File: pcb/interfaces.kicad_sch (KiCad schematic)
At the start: 21 parts, among them J10 BM08B-SRSS-TB, J14 BM03B-SRSS-TB, J3 BM03B-SRSS-TB, J8 BM04B-SRSS-TB, J9 BM04B-SRSS-TB, Q1 MMBT2222A

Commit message: Renamed peripherals to interfaces; added test points; added led jumper
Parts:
- TP29, TP30, TP31, TP32, TP33, TP34, TP35, TP36: value TP -> ~
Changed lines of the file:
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@@
 			)
 		)
-		(property "Value" "TP"
+		(property "Value" "~"
 			(at 113.03 74.168 0)
 			(effects
@@
 			)
 		)
-		(property "Value" "TP"
+		(property "Value" "~"
 			(at 123.19 74.168 0)
 			(effects
@@
 			)
 		)
-		(property "Value" "TP"
+		(property "Value" "~"
 			(at 125.73 74.168 0)
 			(effects
@@
 			)
 		)
-		(property "Value" "TP"
+		(property "Value" "~"
 			(at 118.11 74.168 0)
 			(effects
@@
 			)
 		)
-		(property "Value" "TP"
+		(property "Value" "~"
 			(at 115.57 74.168 0)
 			(effects
@@
 			)
 		)
-		(property "Value" "TP"
+		(property "Value" "~"
 			(at 124.46 17.018 0)
 			(effects
@@
 			)
 		)
-		(property "Value" "TP"
+		(property "Value" "~"
 			(at 127 17.018 0)
 			(effects
@@
 			)
 		)
-		(property "Value" "TP"
+		(property "Value" "~"
 			(at 120.65 74.168 0)
 			(effects

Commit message: Adjusting for consistency
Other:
- title: Hub Hardware -> Aquarius Hub
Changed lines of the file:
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@@
 	(paper "A4")
 	(title_block
-		(title "Hub Hardware")
+		(title "Aquarius Hub")
 		(date "<<release-date>>")
 		(rev "<<tag>>")

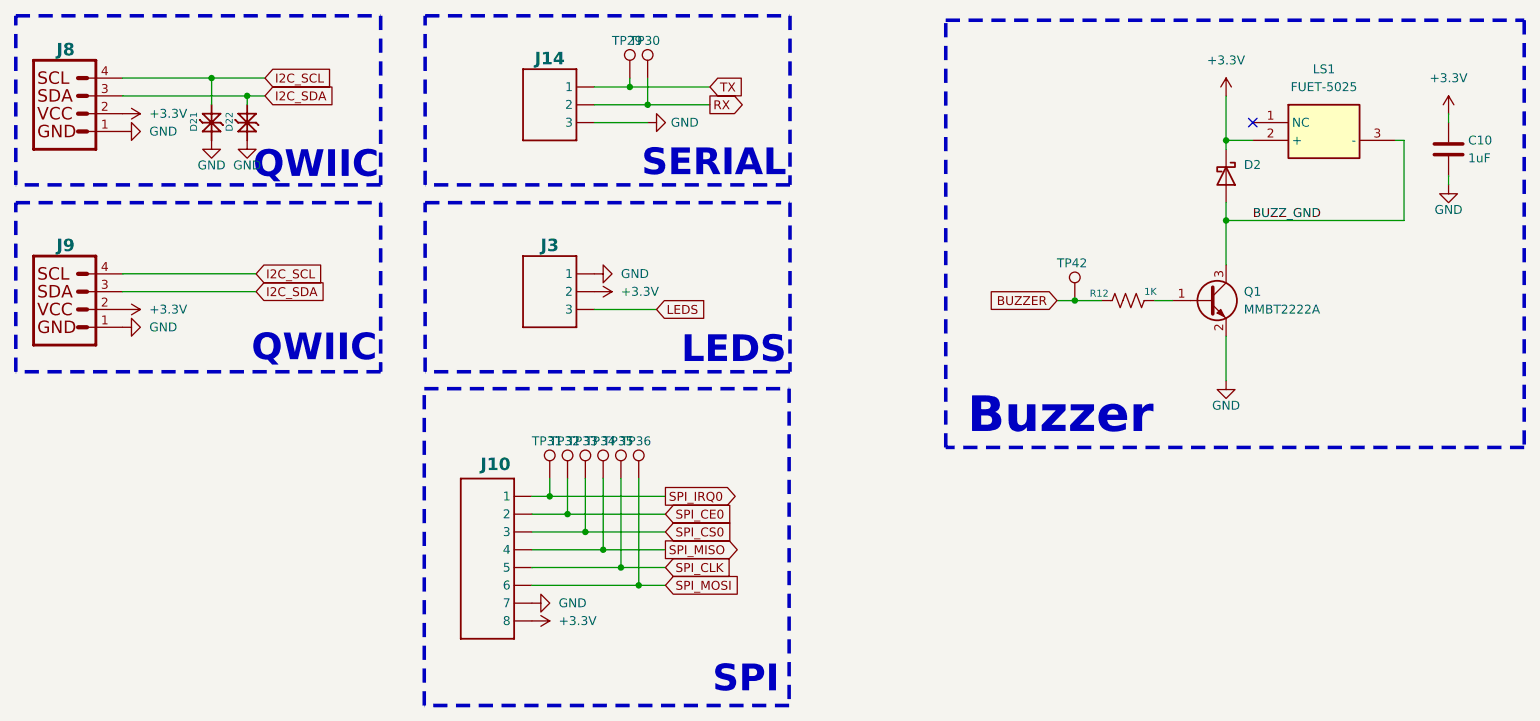
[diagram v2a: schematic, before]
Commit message: Sync symbols and footprints
Transitioned to CRGM footprints
Added dimensions
Fixed some spacing
Adjusted properties
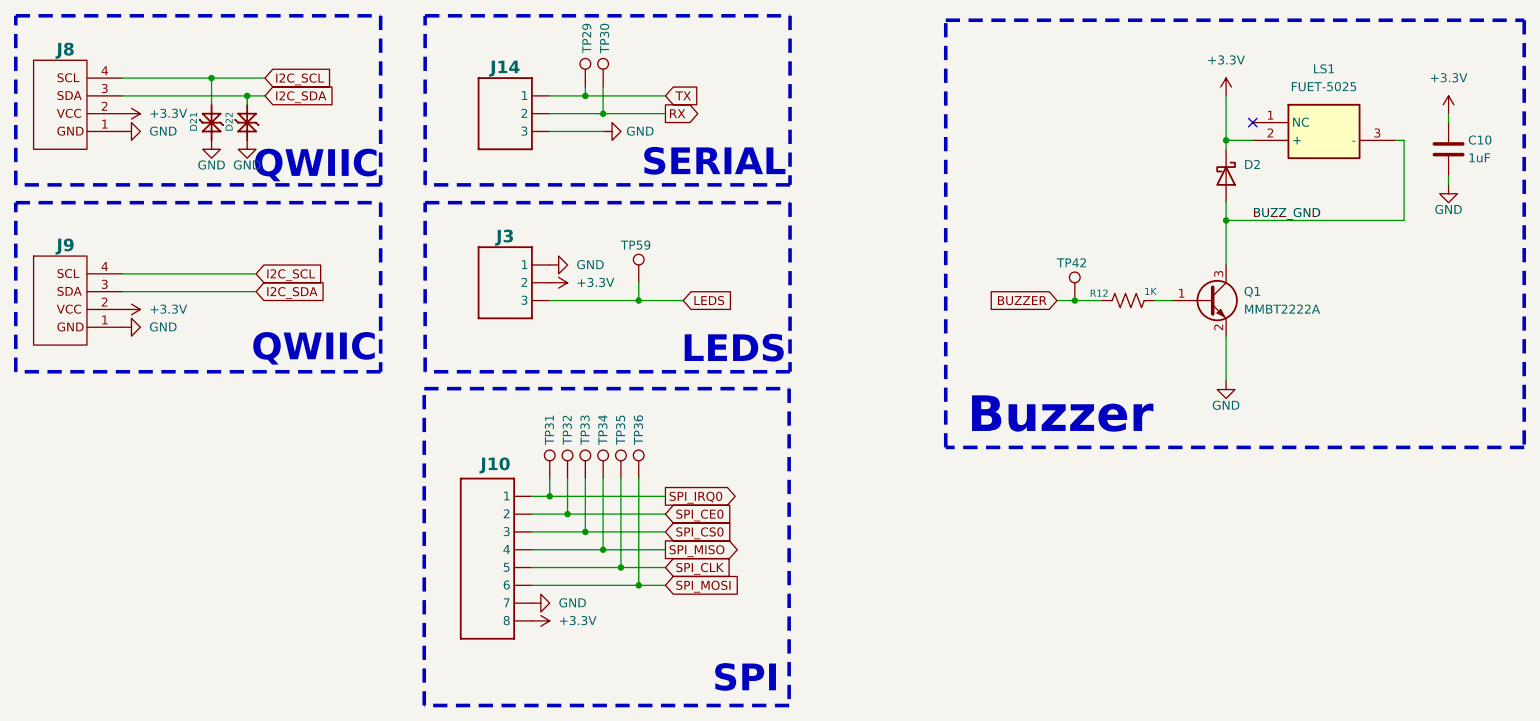
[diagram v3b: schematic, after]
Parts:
- added TP59: ~, CRGM Mechanical:TestPoint_Pad_D1.0mm, symbol Connector:TestPoint
- C10: footprint Capacitor_SMD:C_0603_1608Metric -> CRGM Passive:C_0603_1608Metric
- D2: footprint Diode_SMD:D_SOD-523 -> CRGM Passive:D_SOD-523
- J14, J3: Digikey 455-BM03B-SRSS-TBTR-ND -> 455-BM04B-SRSS-TBTR-ND; LCSC C2919600 -> C2919601; MPN BM03B-SRSS-TB -> BM04B-SRSS-TB; Mouser 306-3BSRSSTBTLP -> 306-BM04BSRSSTBTLFSN
- J8, J9: MPN BM04B-SRSS-TB -> BM04B-SRSS-TBT(LF)(SN)
- Q1: footprint Package_TO_SOT_SMD:SOT-523 -> CRGM Passive:SOT-523
- R12: footprint Resistor_SMD:R_0603_1608Metric -> CRGM Passive:R_0603_1608Metric
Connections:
- net LEDS: now also TP59.1
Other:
- moved on the sheet: J14, J3, TP29, TP30

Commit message: Clean up and consistency
Moved buzzer to MCU
Fixed model directory
Set font size
Set outline size
Upscaled Roxy ❤️
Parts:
- removed C10: 1uF, CRGM Passive:C_0603_1608Metric, symbol Device:C
- removed D2: D_Schottky, CRGM Passive:D_SOD-523, symbol Device:D_Schottky
- removed LS1: FUET-5025, CRG Makes:FUET-5025, symbol CRG Makes:CMT-0502-75-SMT-TR
- removed Q1: MMBT2222A, CRGM Passive:SOT-523, symbol Transistor_BJT:MMBT2222A
- removed R12: 1K, CRGM Passive:R_0603_1608Metric, symbol Device:R_US
- removed TP42: ~, CRGM Mechanical:TestPoint_Pad_D1.0mm, symbol Connector:TestPoint
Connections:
- no-connect marks 1 -> 0
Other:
- note added: "I2C"
- note added: "Serial"
- note removed: "Buzzer"
- note removed: "QWIIC"
- note removed: "SERIAL"

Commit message: fixed LCSC part numbers
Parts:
- J14, J3: LCSC C2919601 -> C2904985
- J8, J9: LCSC C2919601 -> C2904986
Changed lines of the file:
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@@
 			)
 		)
-		(property "LCSC" "C2919601"
+		(property "LCSC" "C2904986"
 			(at 41.656 75.692 0)
 			(effects
@@
 			)
 		)
-		(property "LCSC" "C2919601"
+		(property "LCSC" "C2904985"
 			(at 107.95 43.18 0)
 			(effects
@@
 			)
 		)
-		(property "LCSC" "C2919601"
+		(property "LCSC" "C2904986"
 			(at 41.656 47.752 0)
 			(effects
@@
 			)
 		)
-		(property "LCSC" "C2919601"
+		(property "LCSC" "C2904985"
 			(at 107.95 67.31 0)
 			(effects

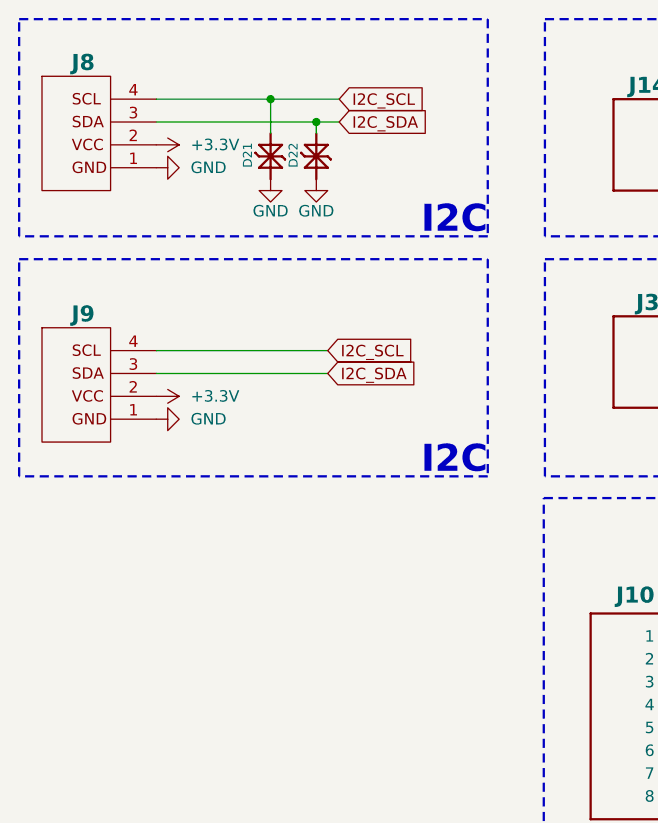
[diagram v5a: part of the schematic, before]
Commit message: Switched to internal and external I2C bus
Updated renders
Updated description of QWICC connectors
Added test points for INT I2C
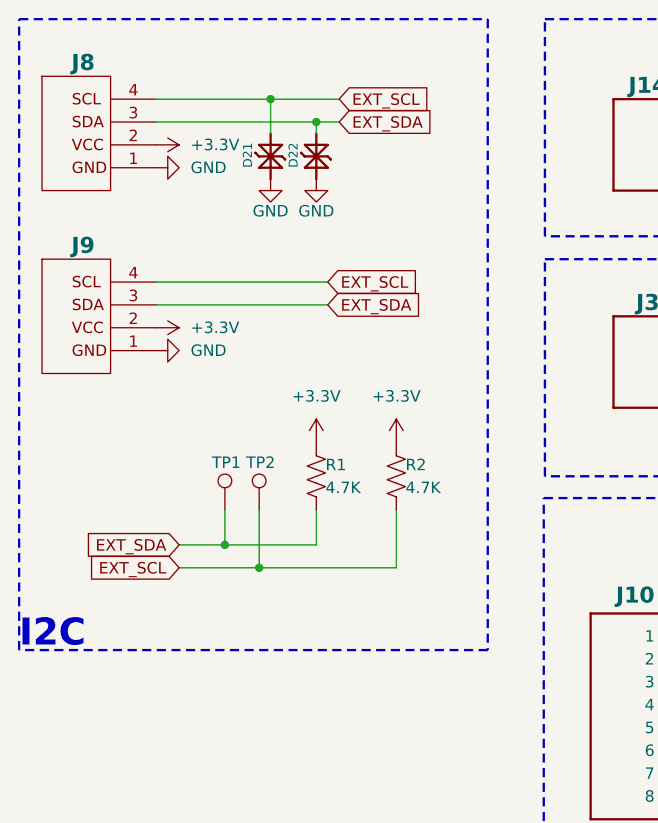
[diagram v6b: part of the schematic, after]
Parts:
- added R1, R2: 4.7K, CRGM Passive:R_0603_1608Metric, symbol Device:R_US
- added TP1, TP2: ~, CRGM Mechanical:TestPoint_Pad_D1.0mm, symbol Connector:TestPoint
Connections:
- net +3.3V: now also R1.1, R2.1
- net I2C_SCL renamed EXT_SCL
- net EXT_SCL: now also R2.2, TP2.1
- net I2C_SDA renamed EXT_SDA
- net EXT_SDA: now also R1.2, TP1.1
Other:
- moved on the sheet: J9

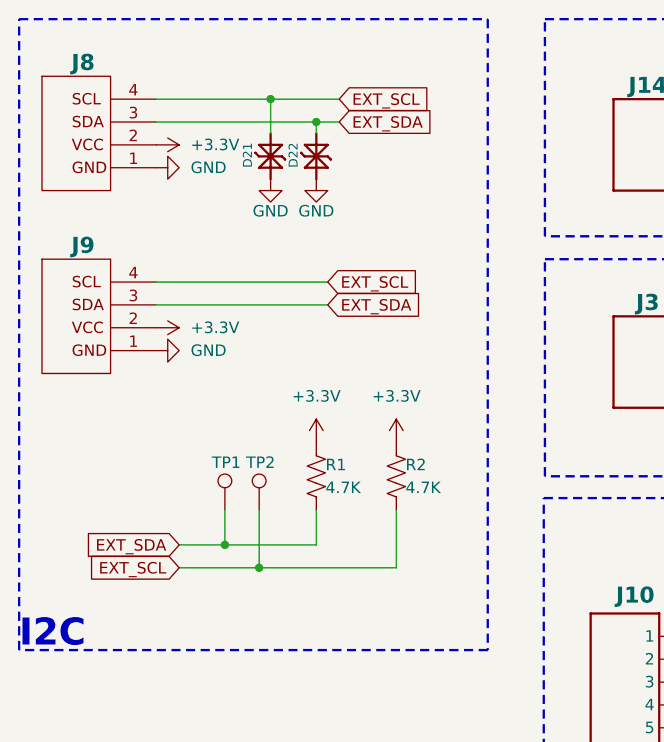
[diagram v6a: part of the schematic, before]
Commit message: Rework to add power connector
Simplified GPIO connectors to make sure for power.
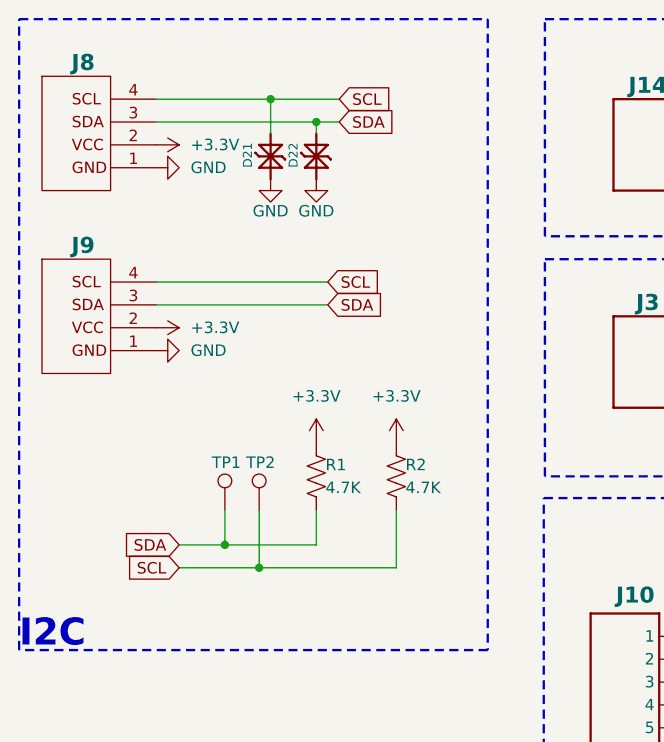
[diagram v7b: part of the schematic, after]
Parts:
- J8, J9: value BM04B-SRSS-TB -> SM04B-SRSS-TB; footprint CRGM Connector:JST_SH_BM04B-SRSS-TB_1x04-1MP_P1.00mm_Vertical -> CRGM Connector:JST_SH_SM04B-SRSS-TB_1x04-1MP_P1.00mm_Horizontal; Digikey 455-BM04B-SRSS-TBTR-ND -> 455-SM04B-SRSS-TBTR-ND; LCSC C2904986 -> C2763614; MPN BM04B-SRSS-TBT(LF)(SN) -> SM04B-SRSS-TBT(LF)(SN); Mouser 306-BM04BSRSSTBTLFSN -> 306-SM04BSRSSTBTLFSN
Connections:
- net EXT_SCL renamed SCL
- net EXT_SDA renamed SDA
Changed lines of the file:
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@@
 		)
 	)
-	(global_label "EXT_SDA"
+	(global_label "SDA"
 		(shape input)
 		(at 52.07 73.66 180)
@@
 		)
 		(property "Intersheetrefs" "${INTERSHEET_REFS}"
-			(at 41.223 73.66 0)
+			(at 45.5167 73.66 0)
 			(effects
 				(font
@@
 		)
 	)
-	(global_label "EXT_SDA"
+	(global_label "SDA"
 		(shape input)
 		(at 69.85 26.67 0)
@@
 		)
 		(property "Intersheetrefs" "${INTERSHEET_REFS}"
-			(at 80.697 26.67 0)
+			(at 76.4033 26.67 0)
 			(effects
 				(font
@@
 		)
 	)
-	(global_label "EXT_SCL"
+	(global_label "SCL"
 		(shape input)
 		(at 69.85 24.13 0)
@@
 		)
 		(property "Intersheetrefs" "${INTERSHEET_REFS}"
-			(at 80.6365 24.13 0)
+			(at 76.3428 24.13 0)
 			(effects
 				(font
@@
 		)
 	)
-	(global_label "EXT_SCL"
+	(global_label "SCL"
 		(shape input)
 		(at 52.07 76.2 180)
@@
 		)
 		(property "Intersheetrefs" "${INTERSHEET_REFS}"
-			(at 41.2835 76.2 0)
+			(at 45.5772 76.2 0)
 			(effects
 				(font
@@
 		)
 	)
-	(global_label "EXT_SCL"
+	(global_label "SCL"
 		(shape input)
 		(at 68.58 44.45 0)
@@
 		)
 		(property "Intersheetrefs" "${INTERSHEET_REFS}"
-			(at 79.3665 44.45 0)
+			(at 75.0728 44.45 0)
 			(effects
 				(font
@@
 		)
 	)
-	(global_label "EXT_SDA"
+	(global_label "SDA"
 		(shape input)
 		(at 68.58 46.99 0)
@@
 		)
 		(property "Intersheetrefs" "${INTERSHEET_REFS}"
-			(at 79.427 46.99 0)
+			(at 75.1333 46.99 0)
 			(effects
 				(font
@@
 			)
 		)
-		(property "Value" "BM04B-SRSS-TB"
+		(property "Value" "SM04B-SRSS-TB"
 			(at 41.275 40.64 0)
 			(effects
@@
 			)
 		)
-		(property "Footprint" "CRGM Connector:JST_SH_BM04B-SRSS-TB_1x04-1MP_P1.00mm_Vertical"
+		(property "Footprint" "CRGM Connector:JST_SH_SM04B-SRSS-TB_1x04-1MP_P1.00mm_Horizontal"
 			(at 41.402 59.944 0)
 			(effects
@@
 			)
 		)
-		(property "MPN" "BM04B-SRSS-TBT(LF)(SN)"
+		(property "MPN" "SM04B-SRSS-TBT(LF)(SN)"
 			(at 41.402 61.976 0)
 			(effects
@@
 			)
 		)
-		(property "LCSC" "C2904986"
+		(property "LCSC" "C2763614"
 			(at 41.656 68.072 0)
 			(effects
@@
 			)
 		)
-		(property "Mouser" "306-BM04BSRSSTBTLFSN"
+		(property "Mouser" "306-SM04BSRSSTBTLFSN"
 			(at 41.91 64.008 0)
 			(effects
@@
 			)
 		)
-		(property "Digikey" "455-BM04B-SRSS-TBTR-ND"
+		(property "Digikey" "455-SM04B-SRSS-TBTR-ND"
 			(at 42.418 66.04 0)
 			(effects
@@
 			)
 		)
-		(property "Value" "BM04B-SRSS-TB"
+		(property "Value" "SM04B-SRSS-TB"
 			(at 41.275 20.32 0)
 			(effects
@@
 			)
 		)
-		(property "Footprint" "CRGM Connector:JST_SH_BM04B-SRSS-TB_1x04-1MP_P1.00mm_Vertical"
+		(property "Footprint" "CRGM Connector:JST_SH_SM04B-SRSS-TB_1x04-1MP_P1.00mm_Horizontal"
 			(at 41.402 39.624 0)
 			(effects
@@
 			)
 		)
-		(property "MPN" "BM04B-SRSS-TBT(LF)(SN)"
+		(property "MPN" "SM04B-SRSS-TBT(LF)(SN)"
 			(at 41.402 41.656 0)
 			(effects
@@
 			)
 		)
-		(property "LCSC" "C2904986"
+		(property "LCSC" "C2763614"
 			(at 41.656 47.752 0)
 			(effects
@@
 			)
 		)
-		(property "Mouser" "306-BM04BSRSSTBTLFSN"
+		(property "Mouser" "306-SM04BSRSSTBTLFSN"
 			(at 41.91 43.688 0)
 			(effects
@@
 			)
 		)
-		(property "Digikey" "455-BM04B-SRSS-TBTR-ND"
+		(property "Digikey" "455-SM04B-SRSS-TBTR-ND"
 			(at 42.418 45.72 0)
 			(effects

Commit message: Moved to vertical connectors
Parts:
- J8, J9: value SM04B-SRSS-TB -> BM04B-SRSS-TB; footprint CRGM Connector:JST_SH_SM04B-SRSS-TB_1x04-1MP_P1.00mm_Horizontal -> CRGM Connector:JST_SH_BM04B-SRSS-TB_1x04-1MP_P1.00mm_Vertical; Digikey 455-SM04B-SRSS-TBTR-ND -> 455-BM04B-SRSS-TBTR-ND; LCSC C2763614 -> C2904986; MPN SM04B-SRSS-TBT(LF)(SN) -> BM04B-SRSS-TBT(LF)(SN); Mouser 306-SM04BSRSSTBTLFSN -> 306-BM04BSRSSTBTLFSN
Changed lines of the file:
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@@
+			)
+		)
+		(property "Package" ""
+			(at 110.49 81.28 90)
+			(effects
+				(font
+					(size 1.27 1.27)
+				)
+				(hide yes)
 			)
 		)
@@
 			)
 		)
+		(property "Package" ""
+			(at 67.31 66.04 0)
+			(effects
+				(font
+					(size 1.27 1.27)
+				)
+				(hide yes)
+			)
+		)
 		(pin "2"
 		)
@@
 		(property "Mouser" ""
 			(at 120.65 81.28 0)
+			(effects
+				(font
+					(size 1.27 1.27)
+				)
+				(hide yes)
+			)
+		)
+		(property "Package" ""
+			(at 120.65 81.28 90)
 			(effects
 				(font
@@
 			)
 		)
+		(property "Package" ""
+			(at 123.19 81.28 90)
+			(effects
+				(font
+					(size 1.27 1.27)
+				)
+				(hide yes)
+			)
+		)
 		(pin "1"
 		)
@@
 			)
 		)
+		(property "Package" ""
+			(at 62.23 30.48 0)
+			(effects
+				(font
+					(size 1.27 1.27)
+				)
+				(hide yes)
+			)
+		)
 		(pin "1"
 		)
@@
 		)
 		(property "Tolerance" "5%"
+			(at 76.2 66.04 0)
+			(effects
+				(font
+					(size 1.27 1.27)
+				)
+				(hide yes)
+			)
+		)
+		(property "Package" ""
 			(at 76.2 66.04 0)
 			(effects
@@
 			)
 		)
+		(property "Package" ""
+			(at 57.15 69.85 0)
+			(effects
+				(font
+					(size 1.27 1.27)
+				)
+				(hide yes)
+			)
+		)
 		(pin "1"
 		)
@@
 			)
 		)
-		(property "Value" "SM04B-SRSS-TB"
+		(property "Value" "BM04B-SRSS-TB"
 			(at 41.275 40.64 0)
 			(effects
@@
 			)
 		)
-		(property "Footprint" "CRGM Connector:JST_SH_SM04B-SRSS-TB_1x04-1MP_P1.00mm_Horizontal"
+		(property "Footprint" "CRGM Connector:JST_SH_BM04B-SRSS-TB_1x04-1MP_P1.00mm_Vertical"
 			(at 41.402 59.944 0)
 			(effects
@@
 			)
 		)
-		(property "MPN" "SM04B-SRSS-TBT(LF)(SN)"
+		(property "MPN" "BM04B-SRSS-TBT(LF)(SN)"
 			(at 41.402 61.976 0)
 			(effects
@@
 			)
 		)
-		(property "LCSC" "C2763614"
+		(property "LCSC" "C2904986"
 			(at 41.656 68.072 0)
 			(effects
@@
 			)
 		)
-		(property "Mouser" "306-SM04BSRSSTBTLFSN"
+		(property "Mouser" "306-BM04BSRSSTBTLFSN"
 			(at 41.91 64.008 0)
 			(effects
@@
 			)
 		)
-		(property "Digikey" "455-SM04B-SRSS-TBTR-ND"
+		(property "Digikey" "455-BM04B-SRSS-TBTR-ND"
 			(at 42.418 66.04 0)
+			(effects
+				(font
+					(size 1.27 1.27)
+				)
+				(hide yes)
+			)
+		)
+		(property "Package" ""
+			(at 36.83 41.91 0)
 			(effects
 				(font
@@
 			)
 		)
+		(property "Package" ""
+			(at 107.95 26.67 0)
+			(effects
+				(font
+					(size 1.27 1.27)
+				)
+				(hide yes)
+			)
+		)
 		(pin "3"
 		)
@@
 			)
 		)
+		(property "Package" ""
+			(at 115.57 81.28 90)
+			(effects
+				(font
+					(size 1.27 1.27)
+				)
+				(hide yes)
+			)
+		)
 		(pin "1"
 		)
@@
 		)
 		(property "Description" "test point"
+			(at 60.96 69.85 0)
+			(effects
+				(font
+					(size 1.27 1.27)
+				)
+				(hide yes)
+			)
+		)
+		(property "Package" ""
 			(at 60.96 69.85 0)
 			(effects
@@
 			)
 		)
+		(property "Package" ""
+			(at 67.31 30.48 0)
+			(effects
+				(font
+					(size 1.27 1.27)
+				)
+				(hide yes)
+			)
+		)
 		(pin "1"
 		)
@@
 			)
 		)
+		(property "Package" ""
+			(at 105.41 81.28 0)
+			(effects
+				(font
+					(size 1.27 1.27)
+				)
+				(hide yes)
+			)
+		)
 		(pin "2"
 		)
@@
 			)
 		)
+		(property "Package" ""
+			(at 123.19 53.34 0)
+			(effects
+				(font
+					(size 1.27 1.27)
+				)
+				(hide yes)
+			)
+		)
 		(pin "1"
 		)
@@
 			)
 		)
-		(property "Value" "SM04B-SRSS-TB"
+		(property "Value" "BM04B-SRSS-TB"
 			(at 41.275 20.32 0)
 			(effects
@@
 			)
 		)
-		(property "Footprint" "CRGM Connector:JST_SH_SM04B-SRSS-TB_1x04-1MP_P1.00mm_Horizontal"
+		(property "Footprint" "CRGM Connector:JST_SH_BM04B-SRSS-TB_1x04-1MP_P1.00mm_Vertical"
 			(at 41.402 39.624 0)
 			(effects
@@
 			)
 		)
-		(property "MPN" "SM04B-SRSS-TBT(LF)(SN)"
+		(property "MPN" "BM04B-SRSS-TBT(LF)(SN)"
 			(at 41.402 41.656 0)
 			(effects
@@
 			)
 		)
-		(property "LCSC" "C2763614"
+		(property "LCSC" "C2904986"
 			(at 41.656 47.752 0)
 			(effects
@@
 			)
 		)
-		(property "Mouser" "306-SM04BSRSSTBTLFSN"
+		(property "Mouser" "306-BM04BSRSSTBTLFSN"
 			(at 41.91 43.688 0)
 			(effects
@@
 			)
 		)
-		(property "Digikey" "455-SM04B-SRSS-TBTR-ND"
+		(property "Digikey" "455-BM04B-SRSS-TBTR-ND"
 			(at 42.418 45.72 0)
+			(effects
+				(font
+					(size 1.27 1.27)
+				)
+				(hide yes)
+			)
+		)
+		(property "Package" ""
+			(at 36.83 21.59 0)
 			(effects
 				(font
@@
 			)
 		)
+		(property "Package" ""
+			(at 107.95 50.8 0)
+			(effects
+				(font
+					(size 1.27 1.27)
+				)
+				(hide yes)
+			)
+		)
 		(pin "3"
 		)
@@
 			)
 		)
+		(property "Package" ""
+			(at 113.03 81.28 90)
+			(effects
+				(font
+					(size 1.27 1.27)
+				)
+				(hide yes)
+			)
+		)
 		(pin "1"
 		)
@@
 			)
 		)
+		(property "Package" ""
+			(at 115.57 25.4 90)
+			(effects
+				(font
+					(size 1.27 1.27)
+				)
+				(hide yes)
+			)
+		)
 		(pin "1"
 		)
@@
 			)
 		)
+		(property "Package" ""
+			(at 118.11 25.4 90)
+			(effects
+				(font
+					(size 1.27 1.27)
+				)
+				(hide yes)
+			)
+		)
 		(pin "1"
 		)
@@
 			(effects
 				(font
+					(size 1.27 1.27)
+				)
+				(hide yes)
+			)
+		)
+		(property "Package" ""
+			(at 118.11 81.28 90)
+			(effects
+				(font
